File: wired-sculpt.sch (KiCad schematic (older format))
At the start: 37 parts, among them J1 10103594-0001LF, J2 FFC3B07-30-T, J3 AVR-ISP-6 - NOT FITTED, Q1 BSS84AK,215, Q2 2N7002BK, SW1 FSMSM, SW2 S2B-PH-K-S(LF)(SN), U1 USBLC6-2SC6, U2 LM2776DBVT, U3 AT90USB1286-AU, Y1 TSX-3225 16.0000MF18X-AC0

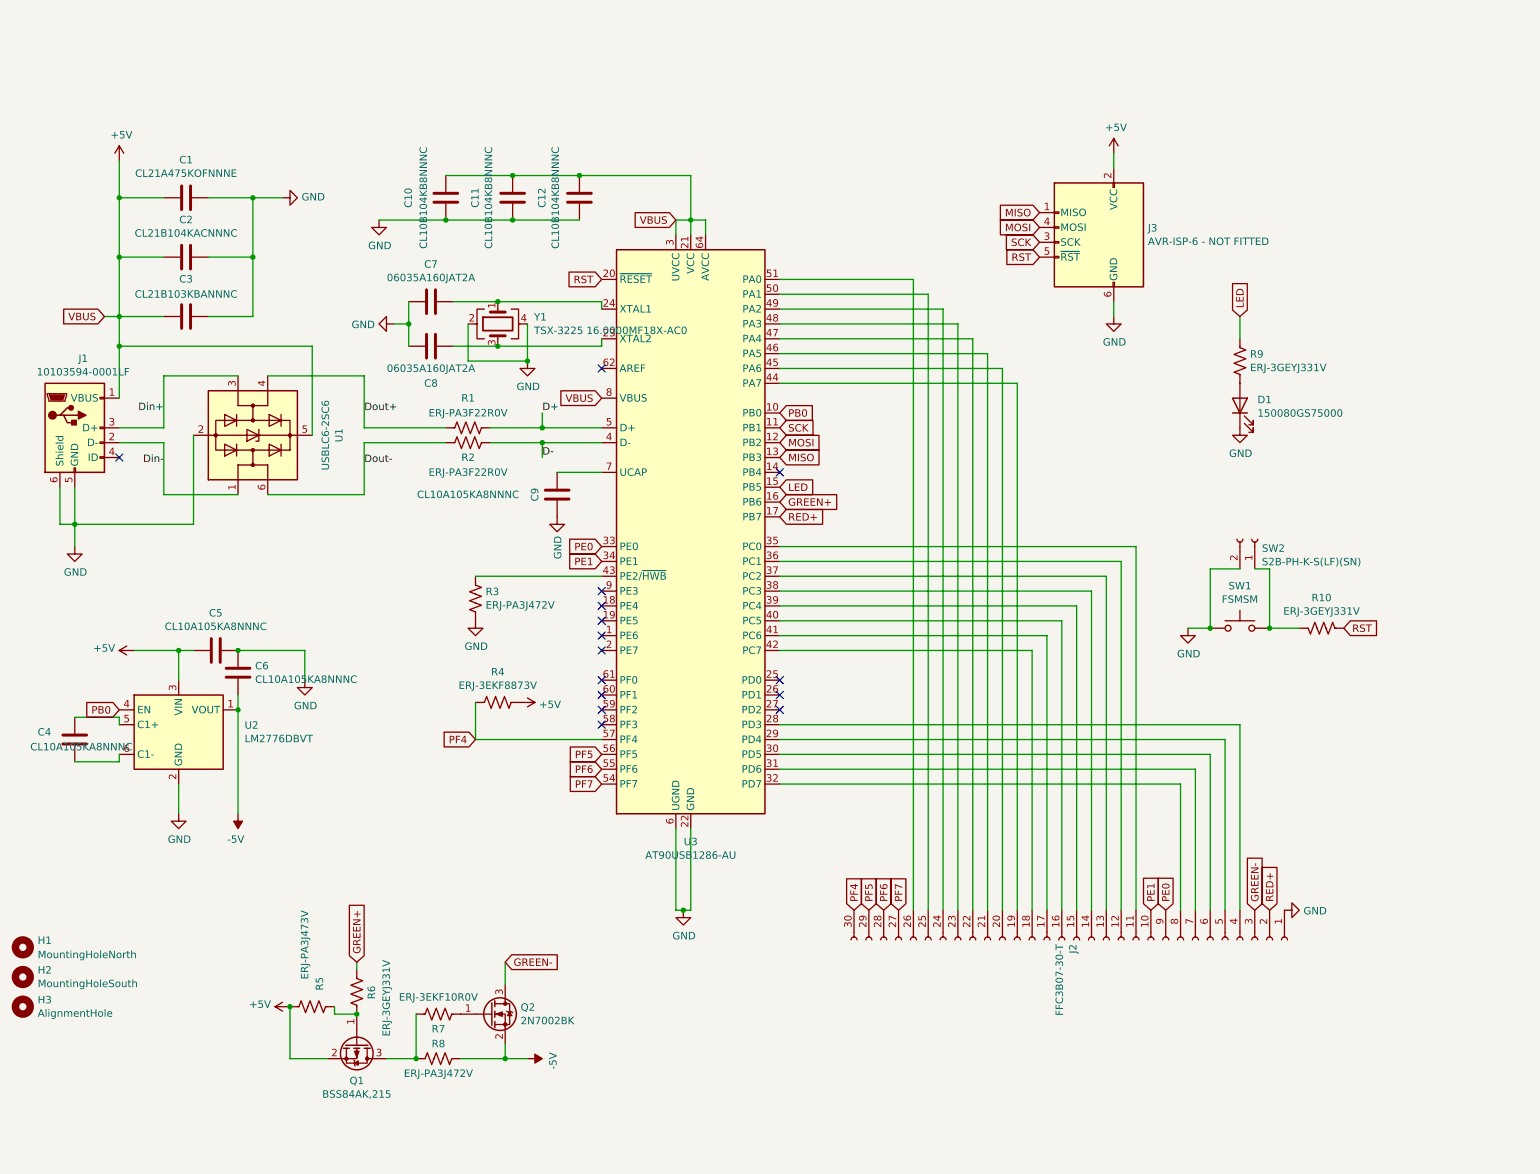
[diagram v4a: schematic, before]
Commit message: Fix Green- and Red+ pins which were backwards. :(
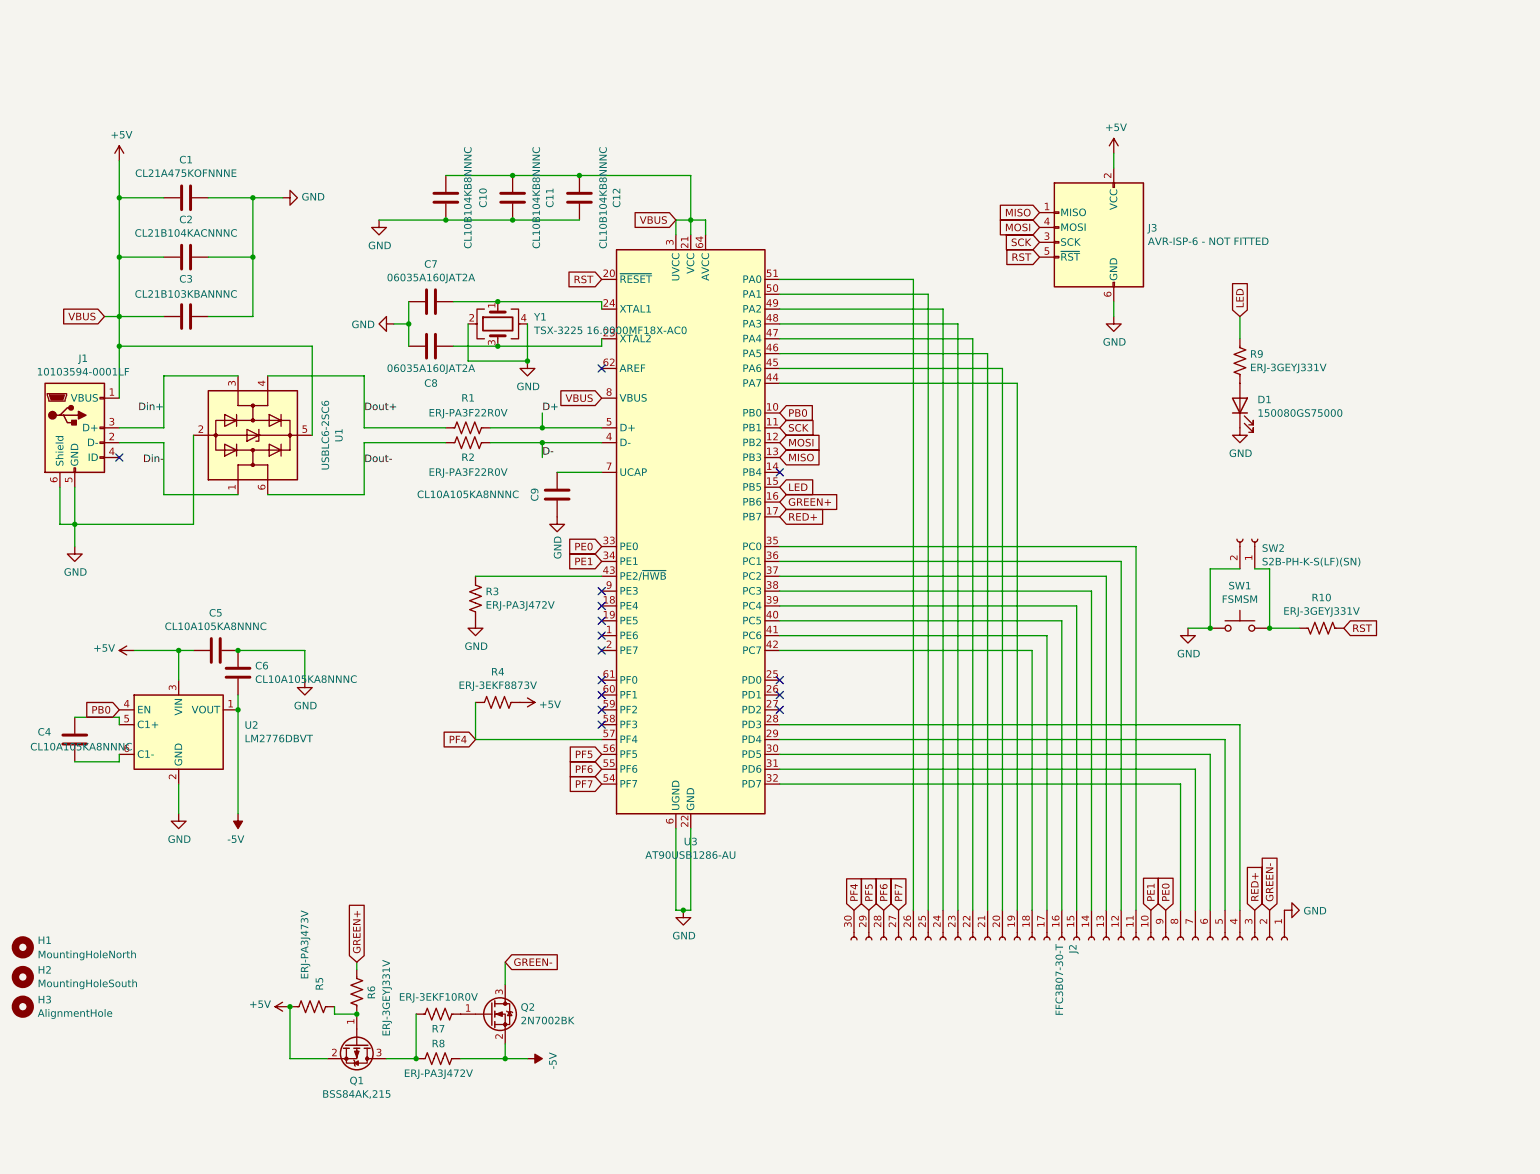
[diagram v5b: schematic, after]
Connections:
- net +5V: now also C10.2, C11.2, C12.2; no longer C10.1, C11.1, C12.1
- net GND: now also C10.1, C11.1, C12.1; no longer C10.2, C11.2, C12.2
- net GREEN-: now also J2.2 (Pin_2); no longer J2.3 (Pin_3)
- net RED+: now also J2.3 (Pin_3); no longer J2.2 (Pin_2)
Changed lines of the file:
@@
 F 3 "https://media.digikey.com/pdf/Data%20Sheets/Samsung%20PDFs/CL05A104KA5NNNC.pdf" H 3900 1150 50  0001 C CNN
 	1    3900 1150
-	1    0    0    -1
+	-1   0    0    1
 $EndComp
 Wire Wire Line
@@
 F 3 "https://media.digikey.com/pdf/Data%20Sheets/Samsung%20PDFs/CL05A104KA5NNNC.pdf" H 4800 1150 50  0001 C CNN
 	1    4800 1150
-	1    0    0    -1
+	-1   0    0    1
 $EndComp
 Text GLabel 5450 1300 0    50   Input ~ 0
@@
 F 3 "https://media.digikey.com/pdf/Data%20Sheets/Samsung%20PDFs/CL05A104KA5NNNC.pdf" H 4350 1150 50  0001 C CNN
 	1    4350 1150
-	1    0    0    -1
+	-1   0    0    1
 $EndComp
 Text GLabel 6650 5950 1    50   Input ~ 0
@@
 Text GLabel 4950 1700 0    50   Input ~ 0
 RST
-Text GLabel 9450 5950 1    50   Input ~ 0
+Text GLabel 9350 5950 1    50   Input ~ 0
 RED+
 NoConn ~ 6150 4500
 NoConn ~ 6150 4600
-Text GLabel 9350 5950 1    50   Input ~ 0
+Text GLabel 9450 5950 1    50   Input ~ 0
 GREEN-
 Text GLabel 6150 3300 2    50   Input ~ 0
@@
 $EndComp
 Wire Wire Line
-	3450 1300 3900 1300
-Wire Wire Line
-	3900 1300 4350 1300
-Connection ~ 3900 1300
-Wire Wire Line
-	4350 1300 4800 1300
-Connection ~ 4350 1300
-Wire Wire Line
-	5550 1000 4800 1000
-Wire Wire Line
 	5550 1000 5550 1300
-Wire Wire Line
-	4800 1000 4350 1000
-Connection ~ 4800 1000
-Wire Wire Line
-	4350 1000 3900 1000
-Connection ~ 4350 1000
 $Comp
 L power:GND #PWR016
@@
 Text GLabel 7900 1250 0    50   Input ~ 0
 MISO
+Wire Wire Line
+	3450 1300 3900 1300
+Connection ~ 3900 1300
+Wire Wire Line
+	3900 1300 4350 1300
+Wire Wire Line
+	3900 1000 4350 1000
+Connection ~ 4350 1300
+Wire Wire Line
+	4350 1300 4800 1300
+Connection ~ 4350 1000
+Wire Wire Line
+	4350 1000 4800 1000
+Connection ~ 4800 1000
+Wire Wire Line
+	4800 1000 5550 1000
 $EndSCHEMATC

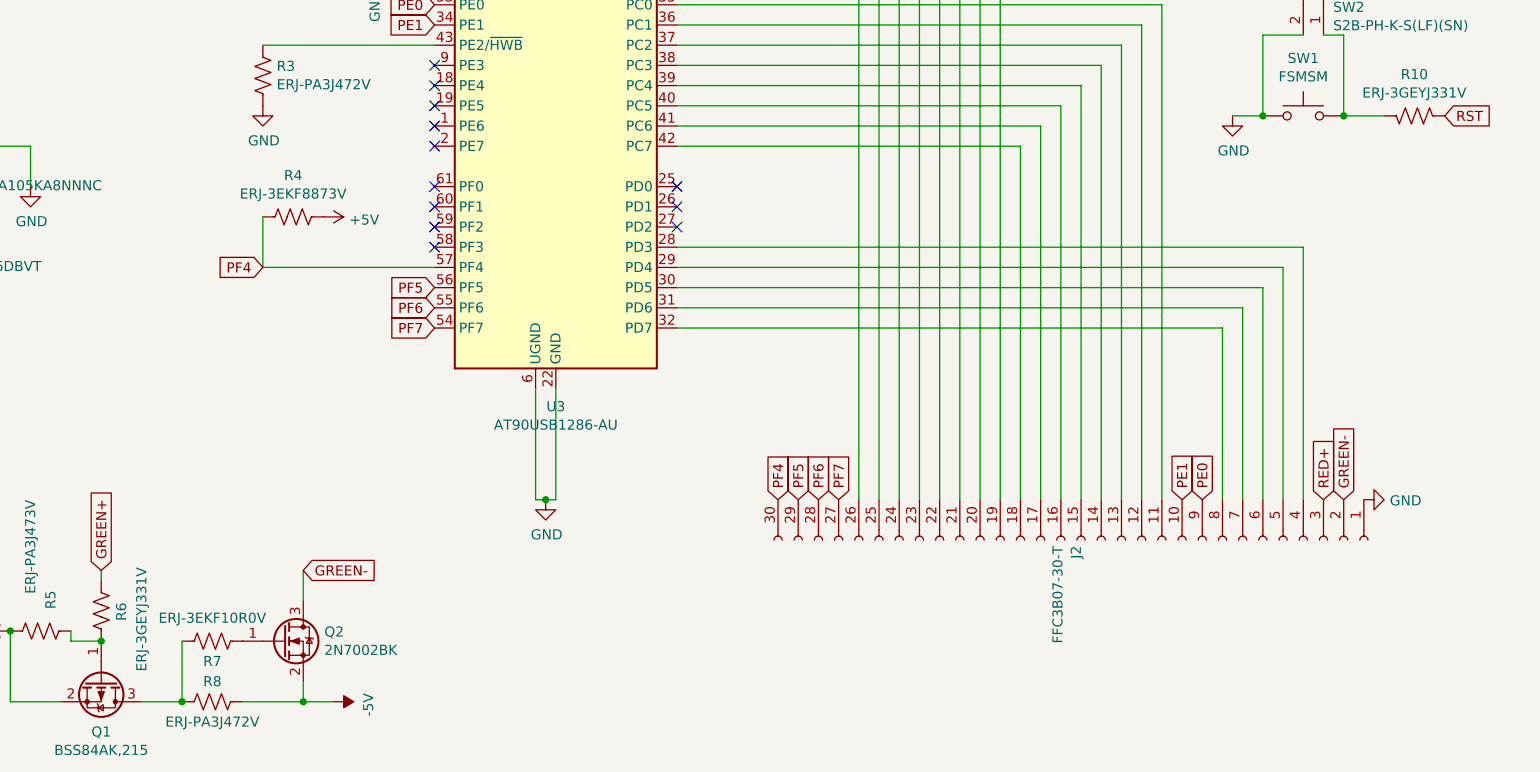
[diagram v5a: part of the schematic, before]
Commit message: add two resistors for the LEDs: this ribbon cable connector must have lower resistance
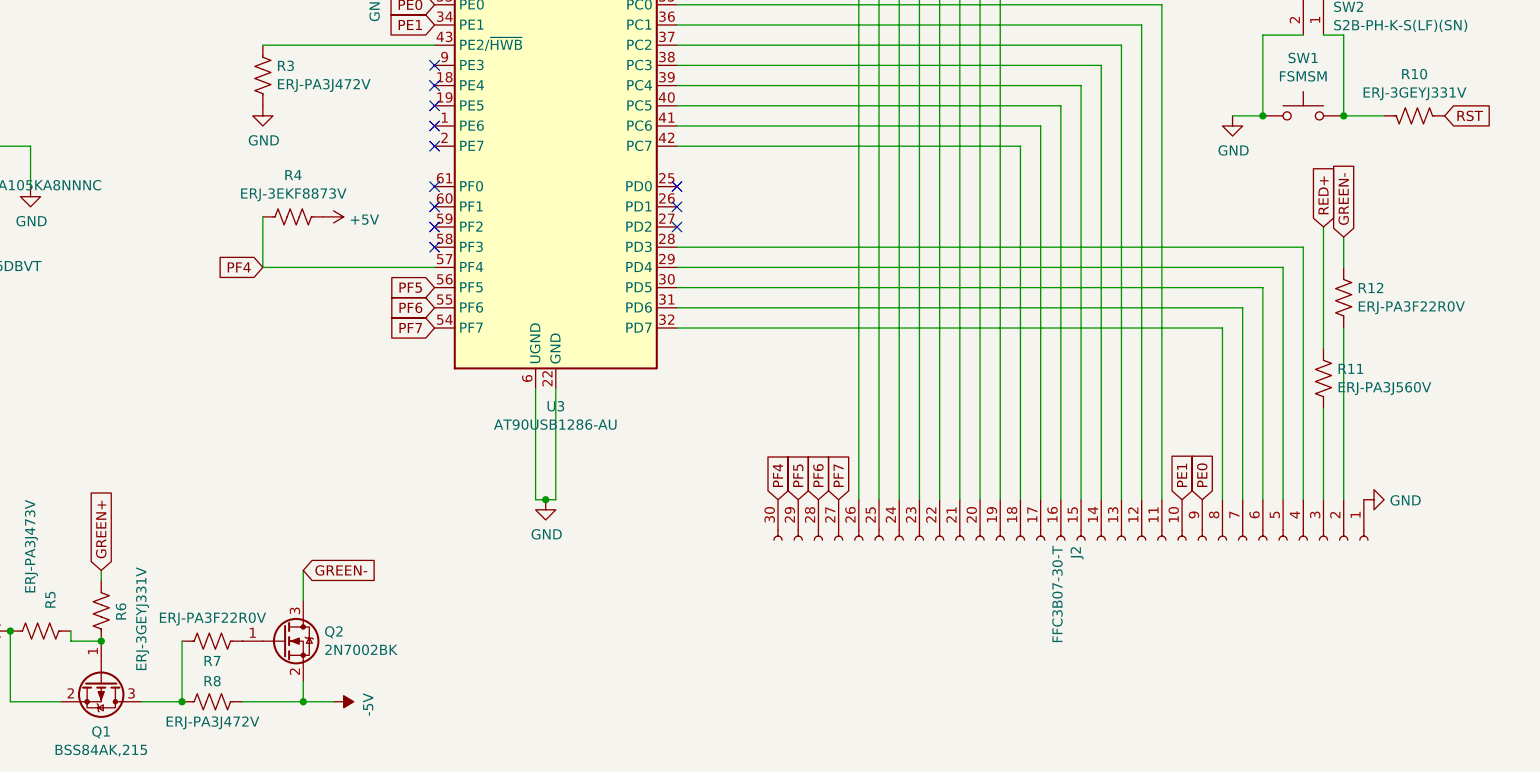
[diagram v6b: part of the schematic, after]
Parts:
- added R11: ERJ-PA3J560V, Resistor_SMD:R_0603_1608Metric, symbol Device:R_US
- added R12: ERJ-PA3F22R0V, Resistor_SMD:R_0603_1608Metric, symbol Device:R_US
- R7: value ERJ-3EKF10R0V -> ERJ-PA3F22R0V
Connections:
- net GREEN-: now also R12.1; no longer J2.2 (Pin_2)
- net RED+: now also R11.1; no longer J2.3 (Pin_3)
- new net: J2.2 (Pin_2), R12.2
- new net: J2.3 (Pin_3), R11.2
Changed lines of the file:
@@
 Text GLabel 4950 1700 0    50   Input ~ 0
 RST
-Text GLabel 9350 5950 1    50   Input ~ 0
+Text GLabel 9350 4600 1    50   Input ~ 0
 RED+
 NoConn ~ 6150 4500
 NoConn ~ 6150 4600
-Text GLabel 9450 5950 1    50   Input ~ 0
+Text GLabel 9450 4650 1    50   Input ~ 0
 GREEN-
 Text GLabel 6150 3300 2    50   Input ~ 0
@@
 P 3850 6650
 F 0 "R7" V 3950 6650 50  0000 C CNN
-F 1 "ERJ-3EKF10R0V" V 3736 6650 50  0000 C CNN
+F 1 "ERJ-PA3F22R0V" V 3736 6650 50  0000 C CNN
 F 2 "Resistor_SMD:R_0603_1608Metric" V 3890 6640 50  0001 C CNN
 F 3 "~" H 3850 6650 50  0001 C CNN
@@
 Wire Wire Line
 	4800 1000 5550 1000
+$Comp
+L Device:R_US R11
+U 1 1 6097A4AF
+P 9350 5350
+F 0 "R11" H 9418 5396 50  0000 L CNN
+F 1 "ERJ-PA3J560V" H 9418 5305 50  0000 L CNN
+F 2 "Resistor_SMD:R_0603_1608Metric" V 9390 5340 50  0001 C CNN
+F 3 "~" H 9350 5350 50  0001 C CNN
+	1    9350 5350
+	1    0    0    -1
+$EndComp
+$Comp
+L Device:R_US R12
+U 1 1 6097BFF6
+P 9450 4950
+F 0 "R12" H 9518 4996 50  0000 L CNN
+F 1 "ERJ-PA3F22R0V" H 9518 4905 50  0000 L CNN
+F 2 "Resistor_SMD:R_0603_1608Metric" V 9490 4940 50  0001 C CNN
+F 3 "~" H 9450 4950 50  0001 C CNN
+	1    9450 4950
+	1    0    0    -1
+$EndComp
+Wire Wire Line
+	9350 4600 9350 5200
+Wire Wire Line
+	9350 5500 9350 5950
+Wire Wire Line
+	9450 5950 9450 5100
+Wire Wire Line
+	9450 4800 9450 4650
 $EndSCHEMATC

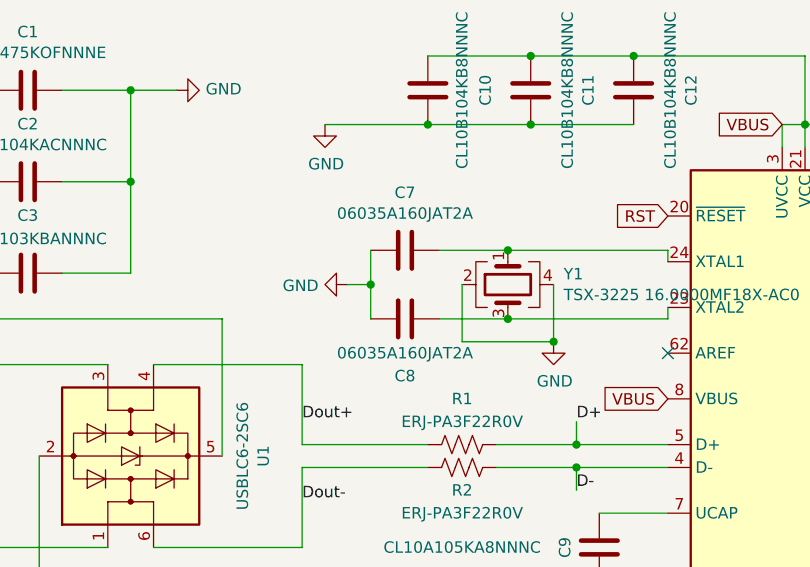
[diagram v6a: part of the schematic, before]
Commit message: chip shortage part substitutions
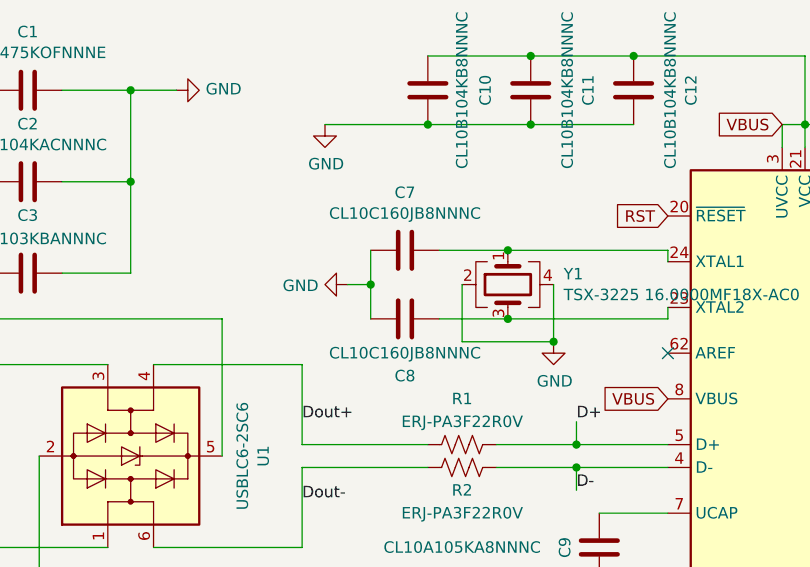
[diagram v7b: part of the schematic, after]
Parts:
- C7, C8: value 06035A160JAT2A -> CL10C160JB8NNNC
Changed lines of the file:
@@
 	1400 3350 1400 3500
-$Comp
-L Device:C C7
-U 1 1 5FC30E75
-P 3800 1850
-F 0 "C7" V 3548 1850 50  0000 C CNN
-F 1 "06035A160JAT2A" V 3639 1850 50  0000 C CNN
-F 2 "Capacitor_SMD:C_0603_1608Metric" H 3838 1700 50  0001 C CNN
-F 3 "~" H 3800 1850 50  0001 C CNN
-	1    3800 1850
-	0    1    1    0
-$EndComp
 $Comp
 L power:GND #PWR06
@@
 P 3800 2150
 F 0 "C8" V 4050 2150 50  0000 C CNN
-F 1 "06035A160JAT2A" V 3950 2150 50  0000 C CNN
+F 1 "CL10C160JB8NNNC" V 3950 2150 50  0000 C CNN
 F 2 "Capacitor_SMD:C_0603_1608Metric" H 3838 2000 50  0001 C CNN
 F 3 "~" H 3800 2150 50  0001 C CNN
@@
 Wire Wire Line
 	9450 4800 9450 4650
+$Comp
+L Device:C C7
+U 1 1 5FC30E75
+P 3800 1850
+F 0 "C7" V 3548 1850 50  0000 C CNN
+F 1 "CL10C160JB8NNNC" V 3639 1850 50  0000 C CNN
+F 2 "Capacitor_SMD:C_0603_1608Metric" H 3838 1700 50  0001 C CNN
+F 3 "~" H 3800 1850 50  0001 C CNN
+	1    3800 1850
+	0    1    1    0
+$EndComp
 $EndSCHEMATC

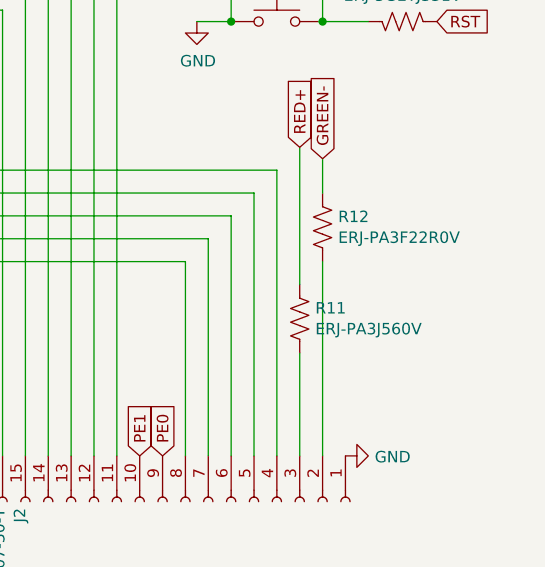
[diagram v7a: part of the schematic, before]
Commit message: change resistor values for LEDs
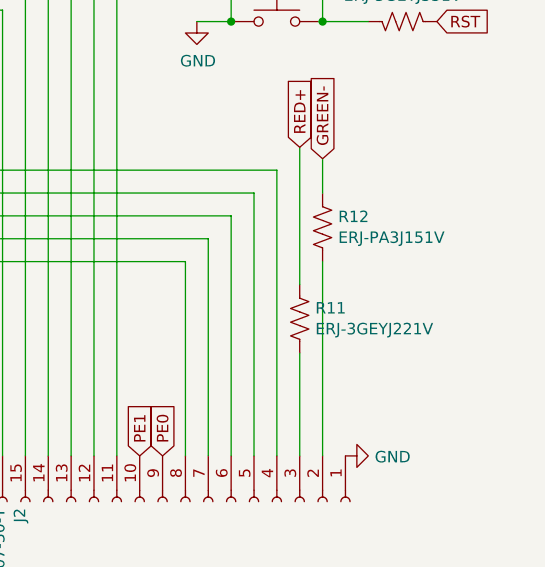
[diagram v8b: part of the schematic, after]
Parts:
- R11: value ERJ-PA3J560V -> ERJ-3GEYJ221V
- R12: value ERJ-PA3F22R0V -> ERJ-PA3J151V
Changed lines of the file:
@@
 P 9350 5350
 F 0 "R11" H 9418 5396 50  0000 L CNN
-F 1 "ERJ-PA3J560V" H 9418 5305 50  0000 L CNN
+F 1 "ERJ-3GEYJ221V" H 9418 5305 50  0000 L CNN
 F 2 "Resistor_SMD:R_0603_1608Metric" V 9390 5340 50  0001 C CNN
 F 3 "~" H 9350 5350 50  0001 C CNN
@@
 P 9450 4950
 F 0 "R12" H 9518 4996 50  0000 L CNN
-F 1 "ERJ-PA3F22R0V" H 9518 4905 50  0000 L CNN
+F 1 "ERJ-PA3J151V" H 9518 4905 50  0000 L CNN
 F 2 "Resistor_SMD:R_0603_1608Metric" V 9490 4940 50  0001 C CNN
 F 3 "~" H 9450 4950 50  0001 C CNN
